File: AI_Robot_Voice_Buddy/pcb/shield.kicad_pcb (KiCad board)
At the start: 2 copper layers, 62 x 64 mm, 15 parts, among them J1 PinSocket_1x19_P2.54mm_Vertic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, J2 PinSocket_1x06_P2.54mm_Vertic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, J3 PinSocket_1x19_P2.54mm_Vertic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, J4 PinSocket_1x05_P2.54mm_Vertic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, J5 PinSocket_1x04_P2.54mm_Vertic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, J6 PinHeader_1x02_P2.54mm_Vertic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, SW1 SW_PUSH_6mm

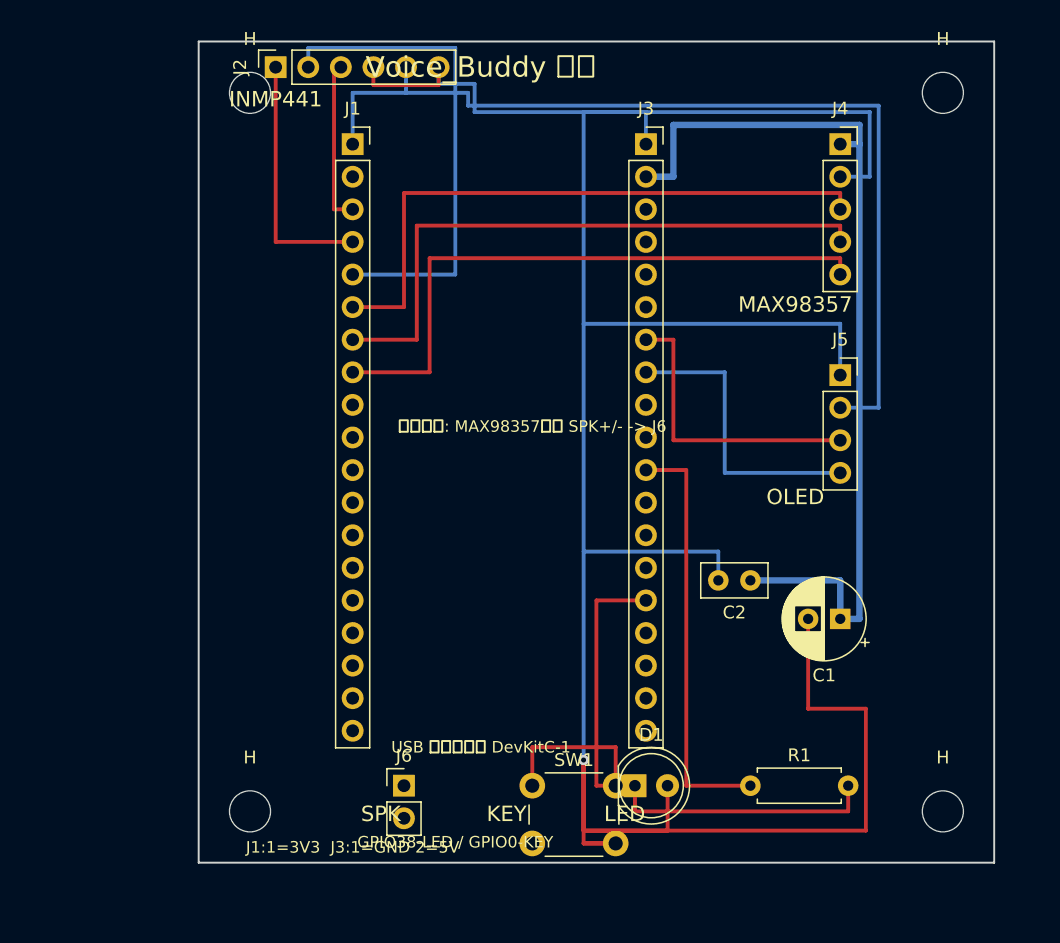
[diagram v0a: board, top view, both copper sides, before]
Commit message: 盾板 v2：KiCad 10.0.6 重制（GND 覆铜 + 官方 DRC）
- gen_pcb.py 适配 KiCad 10 API（VECTOR2I/FromMM/Pads()/board.Add(net)），
  ZONE_FILLER 崩溃问题在 10.0.6 已修复，加回背面整板 GND 覆铜（实心连接）
- 修复官方 DRC 抓出的 v1 隐藏问题（自研检查器采样盲区遗漏）：
  3V3×5V 交叉、SD×3V3 重叠、SD 走廊与焊盘、边缘间距、阻焊桥连、
  钻孔间距（J2 微移 0.5mm）、铜皮孤岛（GND 缝合线）
- DRC 结果：无交叉/短路/间距/阻焊错误；剩余 4 项为已记录豁免
  （zone 几何孤岛——电学上已缝合；安装孔 courtyard×3）
- Gerber 改用 kicad-cli 导出（shield-*.gtl 等标准命名 + shield.drl 单钻文件）
- 渲染 PNG 预览（top/bottom）+ 文档更新；export.py 退役

Co-Authored-By: Claude Code <noreply@anthropic.com>
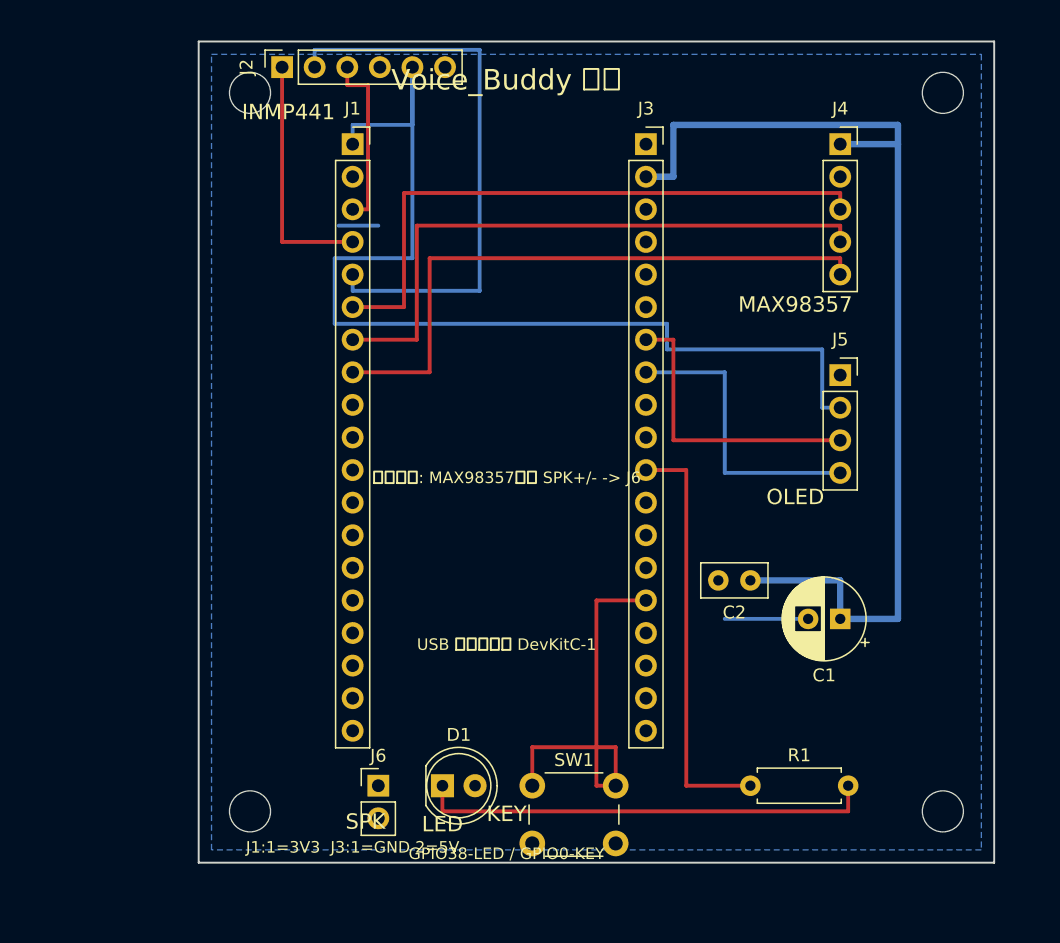
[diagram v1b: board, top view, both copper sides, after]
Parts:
- moved D1 15.0 mm to (19.0, 58.0)
- moved J6 2.00 mm to (14.0, 58.0)
- moved J2 0.50 mm to (6.50, 2.00)
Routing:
- net GND: track 222.5 -> 9.60 mm, vias 1 -> 0
- net LED_A: track 20.6 -> 35.6 mm
- net 5V: track 72.2 -> 81.2 mm
- net 3V3: track 74.5 -> 82.7 mm
- net MIC_SD: track 38.6 -> 44.2 mm
- net MIC_WS: track 13.1 -> 13.9 mm
- net MIC_BCLK: track 19.6 -> 19.1 mm
- added copper zone on B.Cu, net GND

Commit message: 盾板 v2.1：按核查清单补齐（去耦电容/缝合过孔/USB 让位/DRC 清零）
- 板加高 64→68mm：底排元件移到 y=62，避开 DevKitC-1 的 USB-C 接头（y≈59 伸出）
- 新增 C3（INMP441 VDD）/C4（OLED VCC）100nF 去耦电容，就近放置
  （与 C2 共 3 颗 0.1uF，BOM 同步）
- 22 个板边 GND 缝合过孔 + 孤岛缝合链（过孔→F.Cu 走线→J2.4 焊盘）
- C4 位置经 5 轮迭代避开 SCL/SDA/LIGHT 车道与 J3 插座本体
- 官方 DRC：电气类错误（短路/交叉/间距/阻焊桥连）全部清零；
  仅剩安装孔 courtyard×3 与 zone 孤岛提示×1（均有记录豁免）
- 重新导出 Gerber + 钻孔 + 渲染图

Co-Authored-By: Claude Code <noreply@anthropic.com>
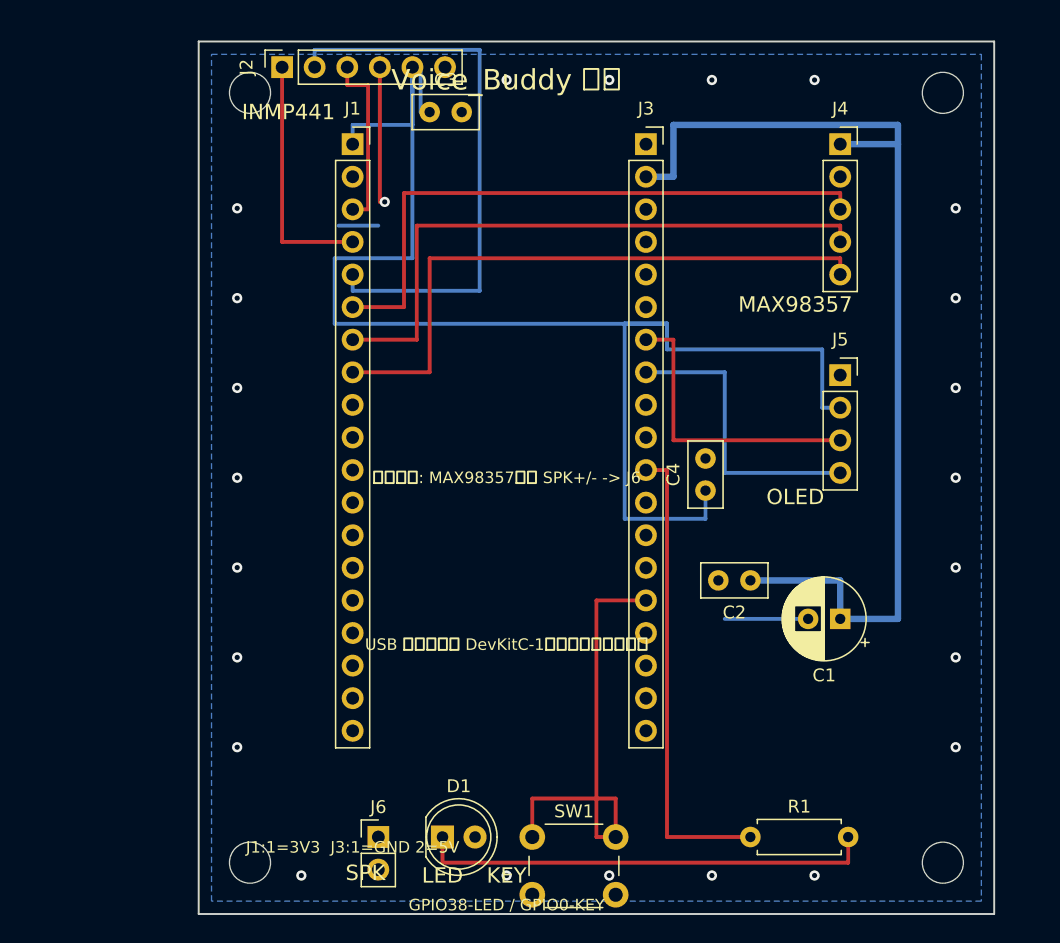
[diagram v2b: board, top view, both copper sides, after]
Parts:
- removed the H at (58.0, 60.0)
- removed the H at (4.00, 60.0)
- added C3: C_Disc_D5.0mm_W2.5mm_P2.50mm, C_Disc_D5.0mm_W2.5mm_P2.50mm, F.Cu at (18.0, 5.50)
- added C4: C_Disc_D5.0mm_W2.5mm_P2.50mm, C_Disc_D5.0mm_W2.5mm_P2.50mm, F.Cu at (39.5, 35.0)
- added H: MountingHole_3.2mm_M3, MountingHole_3.2mm_M3, F.Cu at (58.0, 64.0)
- added H: MountingHole_3.2mm_M3, MountingHole_3.2mm_M3, F.Cu at (4.00, 64.0)
- moved D1 4.00 mm to (19.0, 62.0)
- moved J6 4.00 mm to (14.0, 62.0)
- moved R1 4.00 mm to (43.0, 62.0)
- moved SW1 4.00 mm to (26.0, 62.0)
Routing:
- net 3V3: track 82.7 -> 114.6 mm
- net GND: track 9.60 -> 20.5 mm, vias 0 -> 24
- net LIGHT: track 32.7 -> 36.7 mm
- net KEY: track 32.3 -> 36.3 mm
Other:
- board size 62 x 64 mm -> 62 x 68 mm
- board text added: "USB 口朝下插接 DevKitC-1（底排元件已让位）"
- board text removed: "USB 口朝下插接 DevKitC-1"

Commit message: 盾板 v3：按权威引脚清单重做模块插座（逐脚核验通过）
- J2 圆形 INMP441 2×3 双排母：左列上→下 L/R,WS,SCK；右列上→下 GND,VDD,SD
  （L/R 接 GND、WS→GPIO4、SCK→GPIO5、VDD→3V3、SD→GPIO6）
- J4 MAX98357A 1×7：UIN,GND,SD,GAIN,DIN,BCLK,LRC
  （UIN→3V3、SD/GAIN 悬空、DIN→GPIO7、BCLK→GPIO15、LRC→GPIO16）
- 全板单 3V3 电源：删除 5V 网络；C1 100uF 改 3V3 大容量；C2 移到 J4 UIN 旁
- 去耦就位：C2(J4)/C3(J2)/C4(J5) 各 100nF 跨 3V3↔GND 就近短走线
- OLED 上拉说明：常见模块板载 4.7k；无上拉需手工补焊（文档注明）
- 逐脚网络表程序化核验与规范一一对应；GPIO 映射与固件 config.h 一致
- DRC：电气类错误清零；仅剩 courtyard 组与 2 个纯铜 zone 孤岛（记录豁免）
- 重新导出 Gerber + 钻孔 + 渲染图

Co-Authored-By: Claude Code <noreply@anthropic.com>
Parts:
- J2: value PinSocket_1x06_P2.54mm_Vertical -> PinSocket_2x03_P2.54mm_Vertical; footprint PinSocket_1x06_P2.54mm_Vertical -> PinSocket_2x03_P2.54mm_Vertical
- J4: value PinSocket_1x05_P2.54mm_Vertical -> PinSocket_1x07_P2.54mm_Vertical; footprint PinSocket_1x05_P2.54mm_Vertical -> PinSocket_1x07_P2.54mm_Vertical
- moved C2 38.6 mm to (52.0, 4.50), turned to 90 degrees
- moved J2 7.55 mm to (7.40, 9.50), turned to 180 degrees
- moved C3 5.85 mm to (23.5, 3.50)
- moved C4 2.69 mm to (42.0, 36.0), turned to 0 degrees
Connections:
- C1 pad 1: 5V -> 3V3
- C2 pad 1: 5V -> 3V3
- J2 pad 1: MIC_BCLK -> GND
- J2 pad 2: MIC_SD -> GND
- J2 pad 4: GND -> 3V3
- J2 pad 5: 3V3 -> MIC_BCLK
- J2 pad 6: GND -> MIC_SD
- J3 pad 1: GND -> (no net)
- J3 pad 2: 5V -> (no net)
- J4 pad 1: 5V -> 3V3
- J4 pad 3: AMP_DIN -> (no net)
- J4 pad 4: AMP_BCLK -> (no net)
- J4 pad 5: AMP_LRC -> AMP_DIN
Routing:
- net 3V3: track 114.6 -> 204.0 mm, vias 0 -> 1
- net 5V: track 81.2 -> 0.00 mm
- net AMP_LRC: track 48.2 -> 73.1 mm, vias 0 -> 1
- net GND: track 20.5 -> 6.00 mm, vias 24 -> 22
- net MIC_BCLK: track 19.1 -> 28.1 mm
- net AMP_BCLK: track 48.2 -> 40.5 mm
- net AMP_DIN: track 48.2 -> 43.1 mm
- net MIC_WS: track 13.9 -> 15.7 mm
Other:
- board text added: "INMP441(2x3) 左列:L/R,WS,SCK 右列:GND,VDD,SD"
- board text added: "MAX98357A(1x7) UIN,GND,SD,GAIN,DIN,BCLK,LRC"
- board text added: "OLED 需板载 I2C 上拉（常见模块均有）"
- board text removed: "INMP441"
- board text removed: "J1:1=3V3 J3:1=GND 2=5V"
- board text removed: "MAX98357"
- board text removed: "喇叭飞线: MAX98357模块 SPK+/- -> J6"

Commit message: 盾板 v3.1：C3 去耦移到 J2 VDD 紧邻处（5.5mm）
- C3 竖放 (15.2,5)，SCK 竖线右移 16.5 让位；C3 走线就近接入 3V3 主干
- 满足「每个插座紧邻放置 0.1uF 去耦」：C2(J4 UIN 旁)/C3(J2 VDD 旁 5.5mm)/
  C4(J5 VCC 旁) 全部就位
- DRC 电气类错误保持清零；3 个纯铜 zone 孤岛记录豁免（无悬空焊盘）
- 重新导出 Gerber + 钻孔 + 渲染图

Co-Authored-By: Claude Code <noreply@anthropic.com>
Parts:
- moved C3 8.43 mm to (15.2, 5.00), turned to 90 degrees
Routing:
- net 3V3: track 204.0 -> 194.7 mm, vias 1 -> 0
- net MIC_BCLK: track 28.1 -> 32.3 mm
- net GND: vias 22 -> 23
